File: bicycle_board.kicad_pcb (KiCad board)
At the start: 2 copper layers, 40.9 x 84.4 mm, 156 parts, among them J1 Micro_SD_Card, J10 USB_A, J11 Conn_01x04, J12 Conn_01x01, J13 Conn_01x04, J14 Conn_01x01, J2 USB_C_Receptacle_USB2.0_16P, J3 Conn_01x02, J4 Conn_01x02, J5 Conn_01x08, J6 Conn_01x04, J7 Conn_01x05, J8 Conn_01x02, J9 Conn_01x06, Q1 Q_NMOS_GSD, Q4 Q_NMOS_GSD, Q6 Si2302, Q7 Si2302, Q8 Q_PMOS_GSD, Q9 Q_PMOS_GSD, U1 TP4056, U10 USBLC6-2SC6, U11 BMP280, U12 QMC6308, U13 NS4168, U14 ESP32-C3-WROOM-02U, U15 CH32V203C8T6, U16 PS7516, U17 TXB0108PW, U18 USBLC6-2SC6, U19 QMC7983, U2 SGM2039, U3 ICM-42688-P, U4 QMI8610, U5 AHT20, U6 SGM2033-1.8, U7 74HC595, U8 SGM8040-1, U9 PCA9306DC1, Y1 12MHz, Y2 32.768kHz

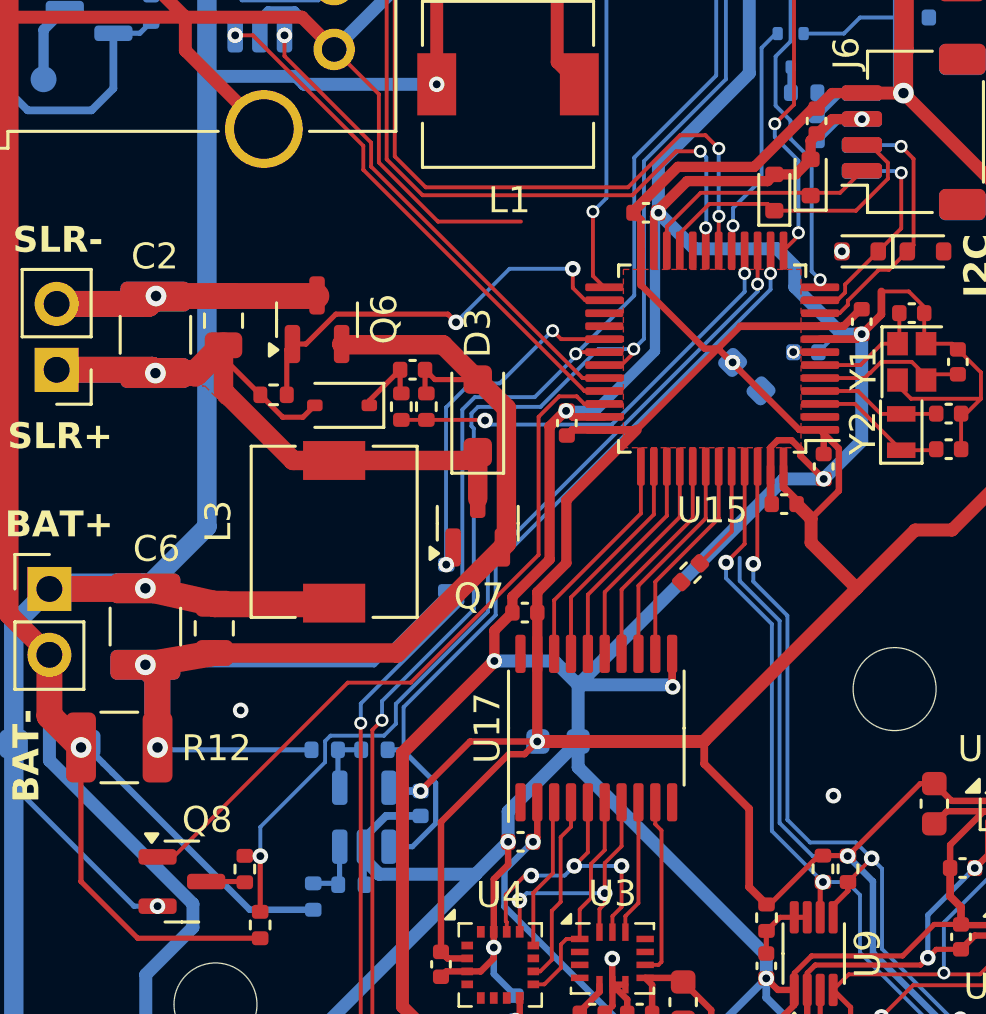
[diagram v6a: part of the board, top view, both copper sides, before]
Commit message: 添加FRAM储存器
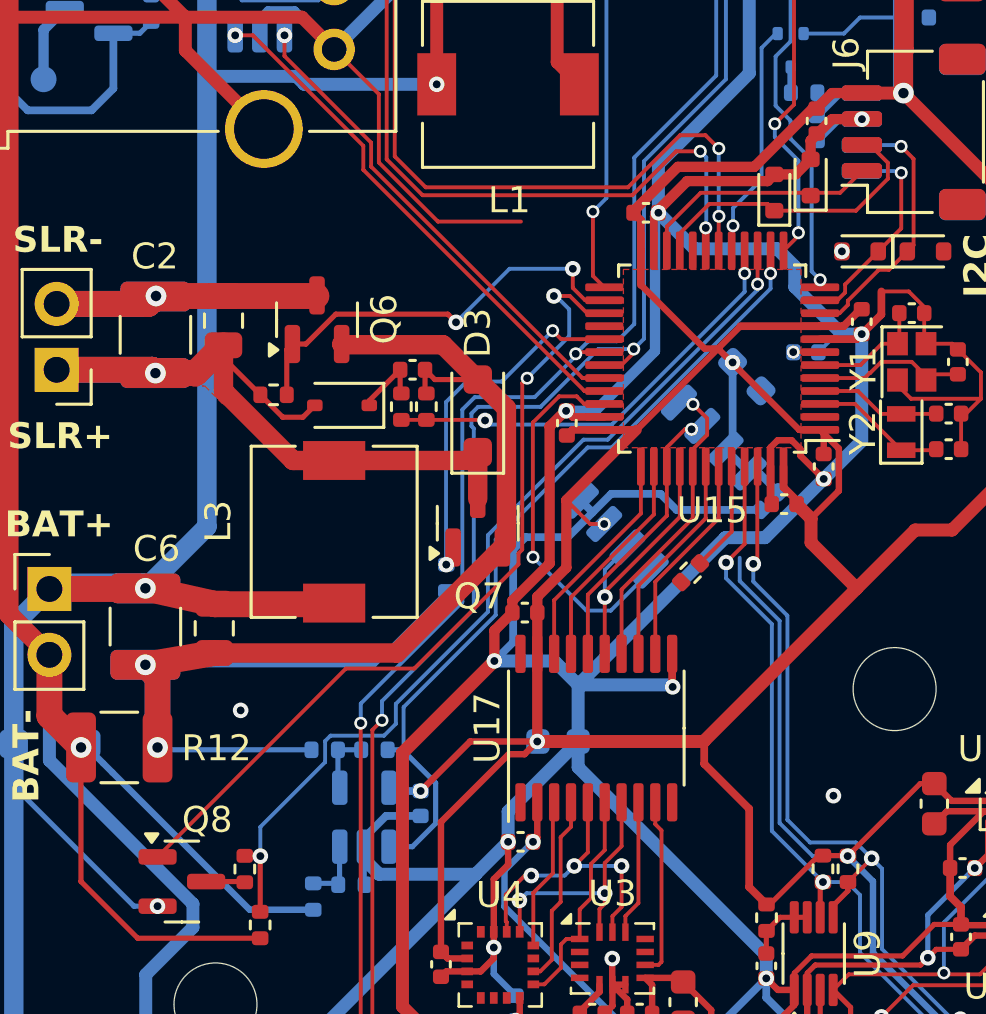
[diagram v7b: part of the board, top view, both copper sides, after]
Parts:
- added C61: 0.1u, Capacitor_SMD:C_0402_1005Metric, B.Cu at (130.8, 112.7)
- added U20: MB85RS256B, Package_SO:SSOP-8_3.9x5.05mm_P1.27mm, B.Cu at (126.8, 112.2)
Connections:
- U15 pad 27: unconnected-(U15-PB14-Pad27) -> /batsamp_en
- U15 pad 34: /batsamp_en -> /SPISen_CS_FRAM
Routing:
- net GND: track 679.7 -> 695.7 mm
- net /SPISen_CS_FRAM: track 0.00 -> 14.5 mm, vias 0 -> 1
- net +3.3V: track 361.0 -> 369.1 mm, vias 11 -> 12
- net /batsamp_en: track 27.8 -> 32.3 mm, vias 0 -> 2
- net /SPISen_MOSI_3V3: track 8.36 -> 11.8 mm, vias 0 -> 1
- net /SPISen_MISO_3V3: track 8.42 -> 10.7 mm, vias 0 -> 1
- net /SPISen_SCLK_3V3: track 8.49 -> 10.5 mm, vias 0 -> 1
- net /TXD: track 78.3 -> 79.0 mm
- net /ADC_Isolar: track 31.3 -> 31.8 mm
- net /ADC_Vbat: track 35.3 -> 35.8 mm
